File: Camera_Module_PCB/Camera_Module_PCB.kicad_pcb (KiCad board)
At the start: 2 copper layers, 84 parts, among them J1 SS-52400-002, J2 Conn_01x02, J3 FFC2A32-24-T, SW1 SW_DIP_x01, SW2 SW_Push, SW3 SW_Push, U2 ESP32-S3R8, U4 MAX98357AETE_T, Y1 40MHz

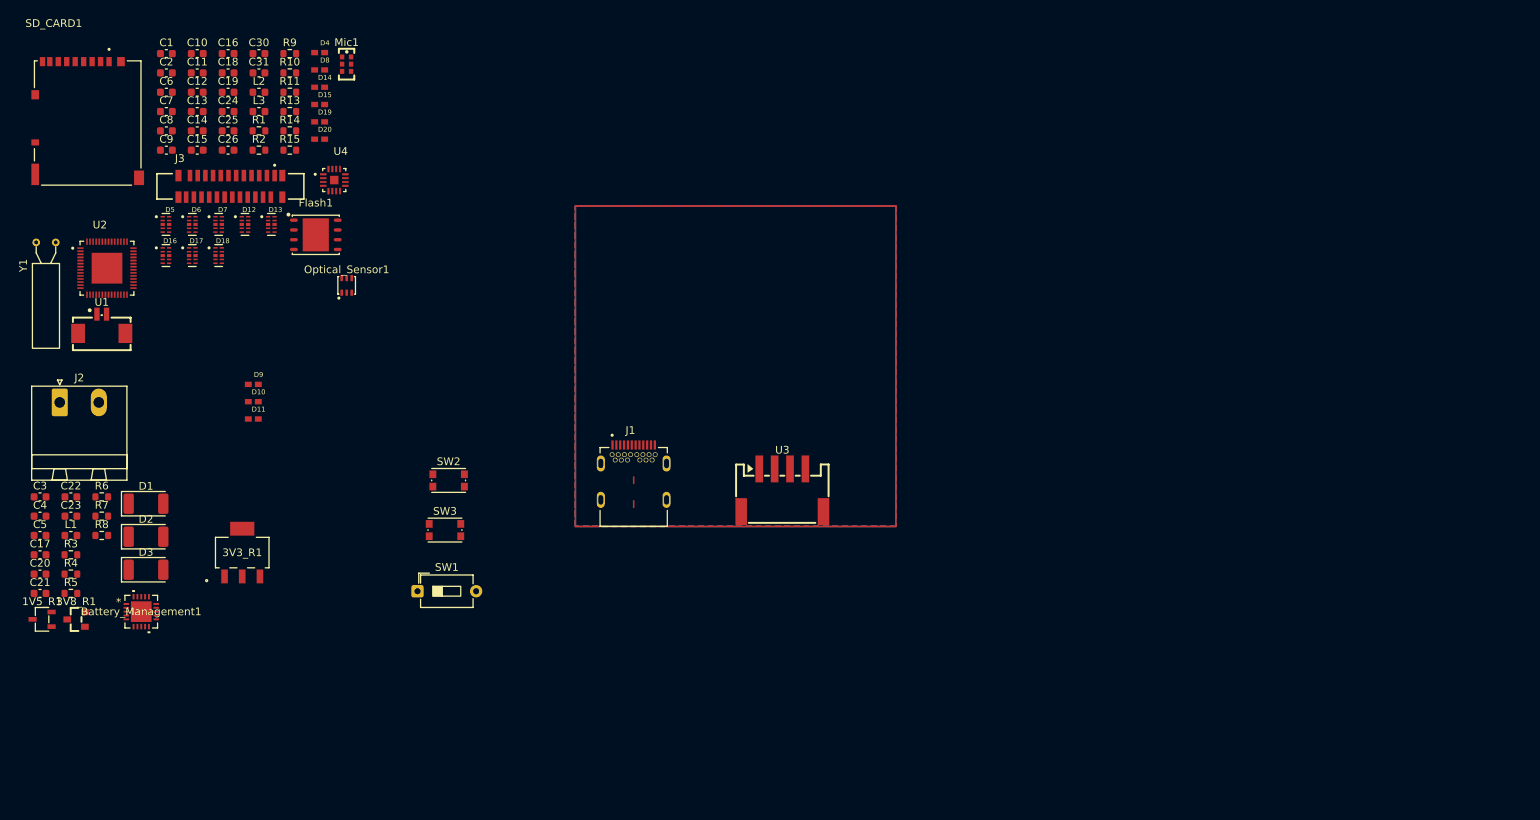
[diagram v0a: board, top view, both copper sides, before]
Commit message: Began early Layout for PCB
Moved most of the ICs into a general area layout for the PCB.
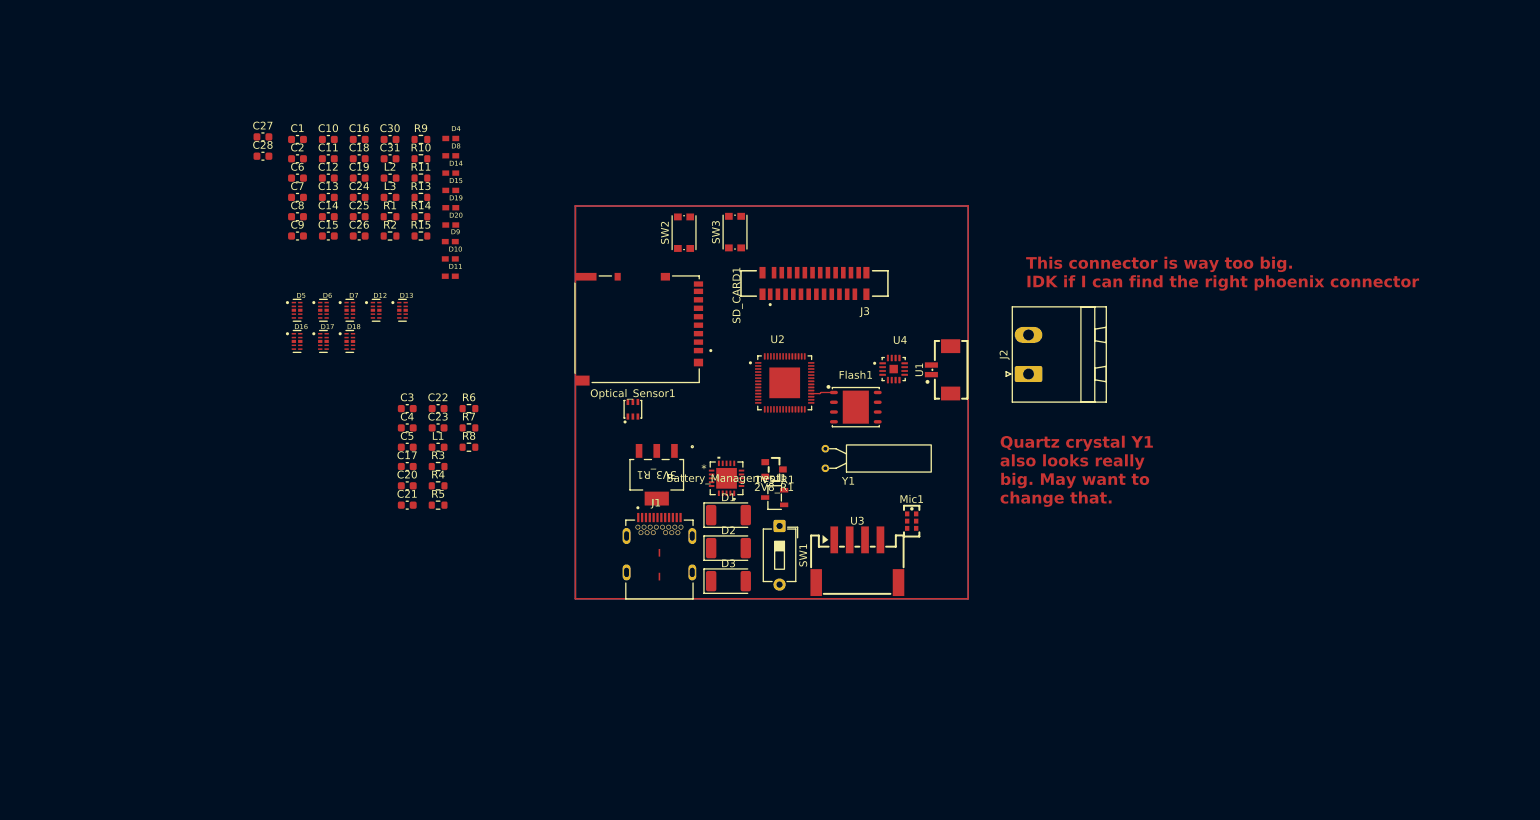
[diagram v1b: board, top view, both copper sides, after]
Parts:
- added C27: 1uF, Capacitor_SMD:C_0603_1608Metric, F.Cu at (61.0, 41.8)
- added C28: 0.1uF, Capacitor_SMD:C_0603_1608Metric, F.Cu at (61.0, 44.3)
- moved J2 126.0 mm to (160.5, 72.6), turned to 90 degrees
- moved U1 109.2 mm to (149.1, 72.1), turned to 90 degrees
- moved Y1 106.7 mm to (134.1, 84.9), turned to 90 degrees
- moved 1V5_R1 96.5 mm to (127.5, 88.7)
- moved Mic1 94.5 mm to (145.3, 91.8)
- moved 2V8_R1 92.8 mm to (127.4, 85.0), turned to 180 degrees
- moved U2 89.3 mm to (128.8, 73.8)
- moved Battery_Management1 78.0 mm to (121.2, 86.2)
- moved J3 77.0 mm to (132.7, 60.9), turned to 180 degrees
- moved U4 76.7 mm to (143.0, 72.0)
- moved SD_CARD1 76.3 mm to (109.6, 66.8), turned to -90 degrees
- moved D1 75.7 mm to (121.5, 91.0)
- moved D2 75.7 mm to (121.5, 95.3)
- moved D3 75.7 mm to (121.5, 99.6)
- moved Flash1 73.7 mm to (138.1, 77.0)
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- renumbered 3V8_R1 to 2V8_R1
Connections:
- U2 pad 29: +3.3V -> /VDD_SPI
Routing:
- net Net-(Flash1-CS): track 0.00 -> 3.01 mm
- removed copper zone on B.Cu, net GND
- removed copper zone on F.Cu, net GND
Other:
- copper layers 2 -> 4
- board text added: "Quartz crystal Y1 also looks really big. May want to change that."
- board text added: "This connector is way too big. IDK if I can find the right phoenix connector"

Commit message: Finished Schematic Except for a small few passives
Finished all of the connections in the schematic page and added a new LED driver. A small selection of passive elements must be given proper values after some calculations.
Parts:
- added C29: 4.7u, Capacitor_SMD:C_0603_1608Metric, F.Cu at (121.0, 40.7)
- added C32: 10uF, Capacitor_SMD:C_0603_1608Metric, F.Cu at (110.0, 40.7)
- added C33: 1uF, Capacitor_SMD:C_0603_1608Metric, F.Cu at (110.0, 43.2)
- added D21: D_Zener, Diode_SMD:D_0603_1608Metric, F.Cu at (47.2, 60.1)
- added D22: LED, LED_SMD:LED_2010_5025Metric, F.Cu at (48.9, 52.4)
- added D23: LED, LED_SMD:LED_2010_5025Metric, F.Cu at (48.9, 56.7)
- added L4: 6.8u, Inductor_SMD:L_0603_1608Metric, F.Cu at (110.0, 45.7)
- added R12: 1k, Resistor_SMD:R_0603_1608Metric, F.Cu at (121.0, 43.2)
- added R16: 25k, Resistor_SMD:R_0603_1608Metric, F.Cu at (121.0, 45.7)
- added R17: Riset, Resistor_SMD:R_0603_1608Metric, F.Cu at (51.2, 60.1)
- added TH1: 10k, Resistor_SMD:R_0603_1608Metric, F.Cu at (57.2, 51.5)
- added U5: AP3032KTR-G1, AP3032KTR-G1:SOT23-6_DIO, F.Cu at (131.5, 42.8)
- D1, D2, D3: footprint LED_SMD:LED_2010_5025Metric -> LED_SMD:LED_0603_1608Metric
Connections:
- Battery_Management1 pad 1: /Power Supply/Charge_Out -> V_OUT_BM
- Battery_Management1 pad 10: unconnected-(Battery_Management1-VSS-Pad10) -> GND
- Battery_Management1 pad 11: unconnected-(Battery_Management1-VSS-Pad11) -> GND
- Battery_Management1 pad 12: unconnected-(Battery_Management1-PROG3-Pad12) -> Net-(Battery_Management1-PROG3)
- Battery_Management1 pad 13: unconnected-(Battery_Management1-PROG1-Pad13) -> Net-(Battery_Management1-PROG1)
- Battery_Management1 pad 21: unconnected-(Battery_Management1-EP-Pad21) -> GND
- Battery_Management1 pad 5: unconnected-(Battery_Management1-THERM-Pad5) -> Net-(Battery_Management1-THERM)
- U2 pad 38: unconnected-(U2-GPIO33-Pad38) -> /LED_CT

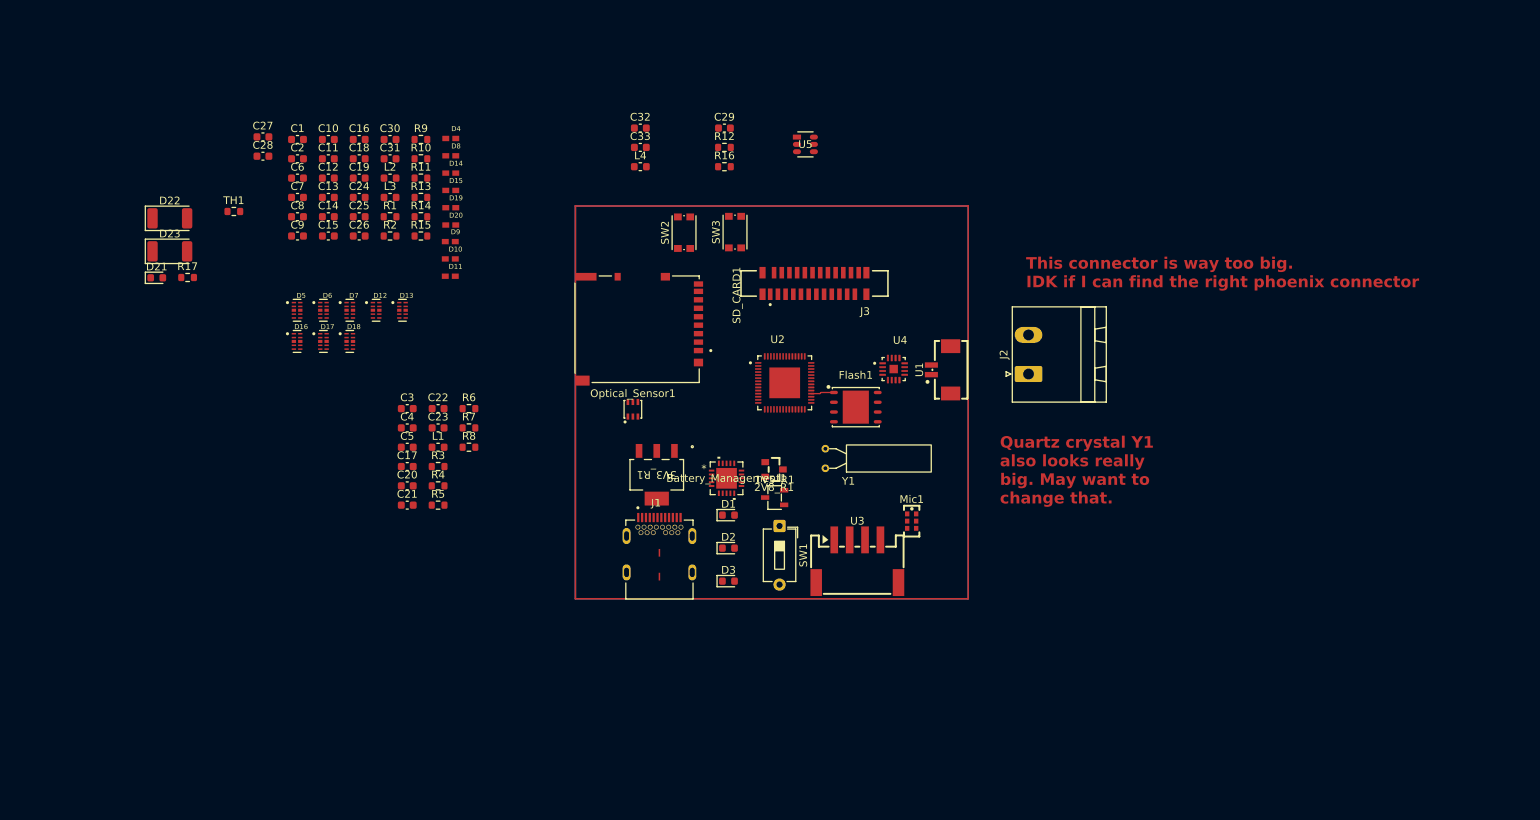
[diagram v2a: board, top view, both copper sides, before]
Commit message: Added Most ICs to the General PCB Layout
Most of the intended ICs that are going to be used were put into a general IC layout. A decision will need to be made in regards to the antenna. The ESP32 Model that is being used may be replaced, or remain the same.
Once the decision is made, more can be added.
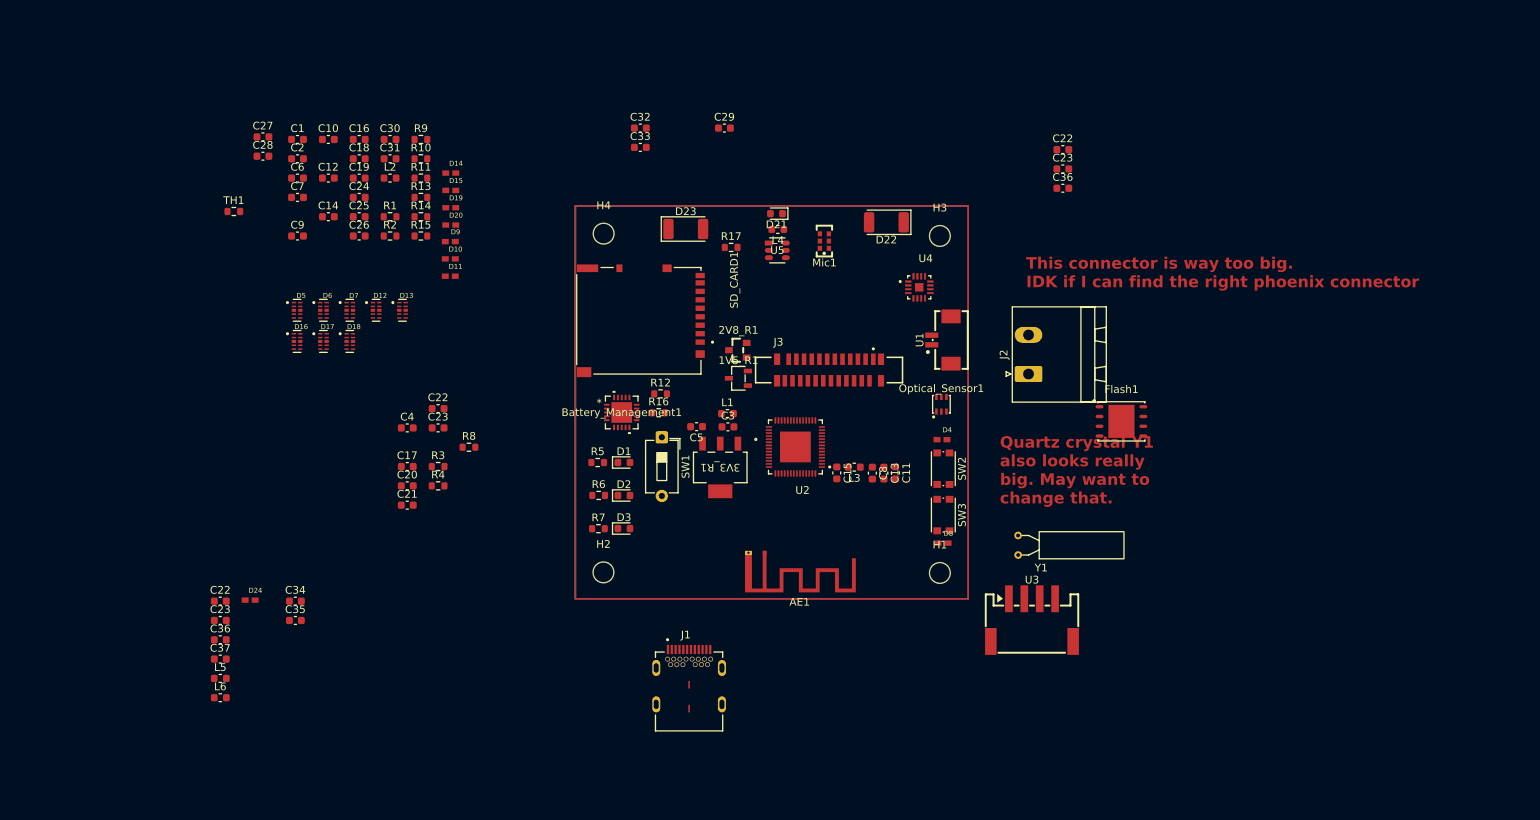
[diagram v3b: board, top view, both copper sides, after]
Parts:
- added AE1: Antenna, RF_Antenna:Texas_SWRA117D_2.4GHz_Left, F.Cu at (126.2, 95.9)
- added C22: C_Small, Capacitor_SMD:C_0603_1608Metric, F.Cu at (55.5, 102.2)
- added C22: NG, Capacitor_SMD:C_0603_1608Metric, F.Cu at (165.0, 43.5)
- added C23: C_Small, Capacitor_SMD:C_0603_1608Metric, F.Cu at (55.5, 104.7)
- added C23: 1.8pF, Capacitor_SMD:C_0603_1608Metric, F.Cu at (165.0, 46.0)
- added C34: 1 uF, Capacitor_SMD:C_0603_1608Metric, F.Cu at (65.2, 102.2)
- added C35: 100 nF, Capacitor_SMD:C_0603_1608Metric, F.Cu at (65.2, 104.7)
- added C36: 1pF, Capacitor_SMD:C_0603_1608Metric, F.Cu at (165.0, 48.5)
- added C36: C_Small, Capacitor_SMD:C_0603_1608Metric, F.Cu at (55.5, 107.2)
- added C37: C_Small, Capacitor_SMD:C_0603_1608Metric, F.Cu at (55.5, 109.7)
- added D24: 0402ESDA-MLP1, ESP32CAM_Foorprints:ESD_0402ESDA-MLP1, F.Cu at (59.3, 102.0)
- added H1: MountingHole, MountingHole:MountingHole_2.7mm, F.Cu at (149.0, 98.5)
- added H2: MountingHole, MountingHole:MountingHole_2.7mm, F.Cu at (105.2, 98.4)
- added H3: MountingHole, MountingHole:MountingHole_2.7mm, F.Cu at (149.0, 54.7)
- added H4: MountingHole, MountingHole:MountingHole_2.7mm, F.Cu at (105.3, 54.4)
- added L5: L, Inductor_SMD:L_0603_1608Metric, F.Cu at (55.5, 112.2)
- added L6: L, Inductor_SMD:L_0603_1608Metric, F.Cu at (55.5, 114.7)
- R17: value Riset -> 10
- moved D22 93.1 mm to (142.0, 52.9), turned to 180 degrees
- moved C11 84.3 mm to (143.2, 85.5), turned to -90 degrees
- moved C8 81.8 mm to (140.2, 85.5), turned to -90 degrees
- moved D8 81.4 mm to (149.4, 94.6)
- moved D21 81.0 mm to (127.7, 51.8), turned to 180 degrees
- moved C13 80.6 mm to (141.7, 85.5), turned to -90 degrees
- moved D4 74.9 mm to (149.2, 81.2)
- moved C15 72.9 mm to (135.6, 85.5), turned to -90 degrees
- moved R17 70.8 mm to (121.8, 56.2)
- moved L3 69.8 mm to (137.8, 84.8), turned to 180 degrees
- moved D23 67.1 mm to (116.0, 53.8)
- moved SW3 45.7 mm to (149.4, 91.0), turned to -90 degrees
- moved SW2 45.6 mm to (149.4, 85.0), turned to -90 degrees
- moved C3 41.7 mm to (121.4, 79.5)
- moved Optical_Sensor1 40.1 mm to (149.2, 76.6)
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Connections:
- 1V5_R1 pad 2: /Power Supply/VDD_1V5 -> VDD_1V5
- 2V8_R1 pad 2: +3.3V -> AVDD_2V8
- 2V8_R1 pad 3: /Power Supply/AVDD_2V8 -> +3.3V
- D10 pad 1: /Power Supply/USB_D+ -> /USB_D+
- D19 pad 2: Net-(U2-U0RXD) -> Net-(U2-U0TXD)
- D9 pad 1: /Power Supply/USB_D- -> /USB_D-
- J1 pad A6: /Power Supply/USB_D+ -> /USB_D+
- J1 pad A7: /Power Supply/USB_D- -> /USB_D-
- J1 pad B6: /Power Supply/USB_D+ -> /USB_D+
- J1 pad B7: /Power Supply/USB_D- -> /USB_D-
- J3 pad 10: /VDD_1V5 -> VDD_1V5
- J3 pad 11: /AVDD_2V8 -> AVDD_2V8
- J3 pad 4: /AVDD_2V8 -> AVDD_2V8
- R13 pad 1: /AVDD_2V8 -> AVDD_2V8
- U2 pad 1: unconnected-(U2-LNA_IN-Pad1) -> /LNA_IN
- U2 pad 37: /IR_DIM -> /LED_CT
- U2 pad 38: /LED_CT -> unconnected-(U2-GPIO33-Pad38)
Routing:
- net Net-(Flash1-CS): track 3.01 -> 0.00 mm
- added copper zone on In1.Cu, net GND
- added copper zone on In2.Cu, net GND

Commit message: MCU Layout Started
The layout for the ESP32 has been started, according to the recommended 4-Layer layout. Please look over the antenna and continue layout.
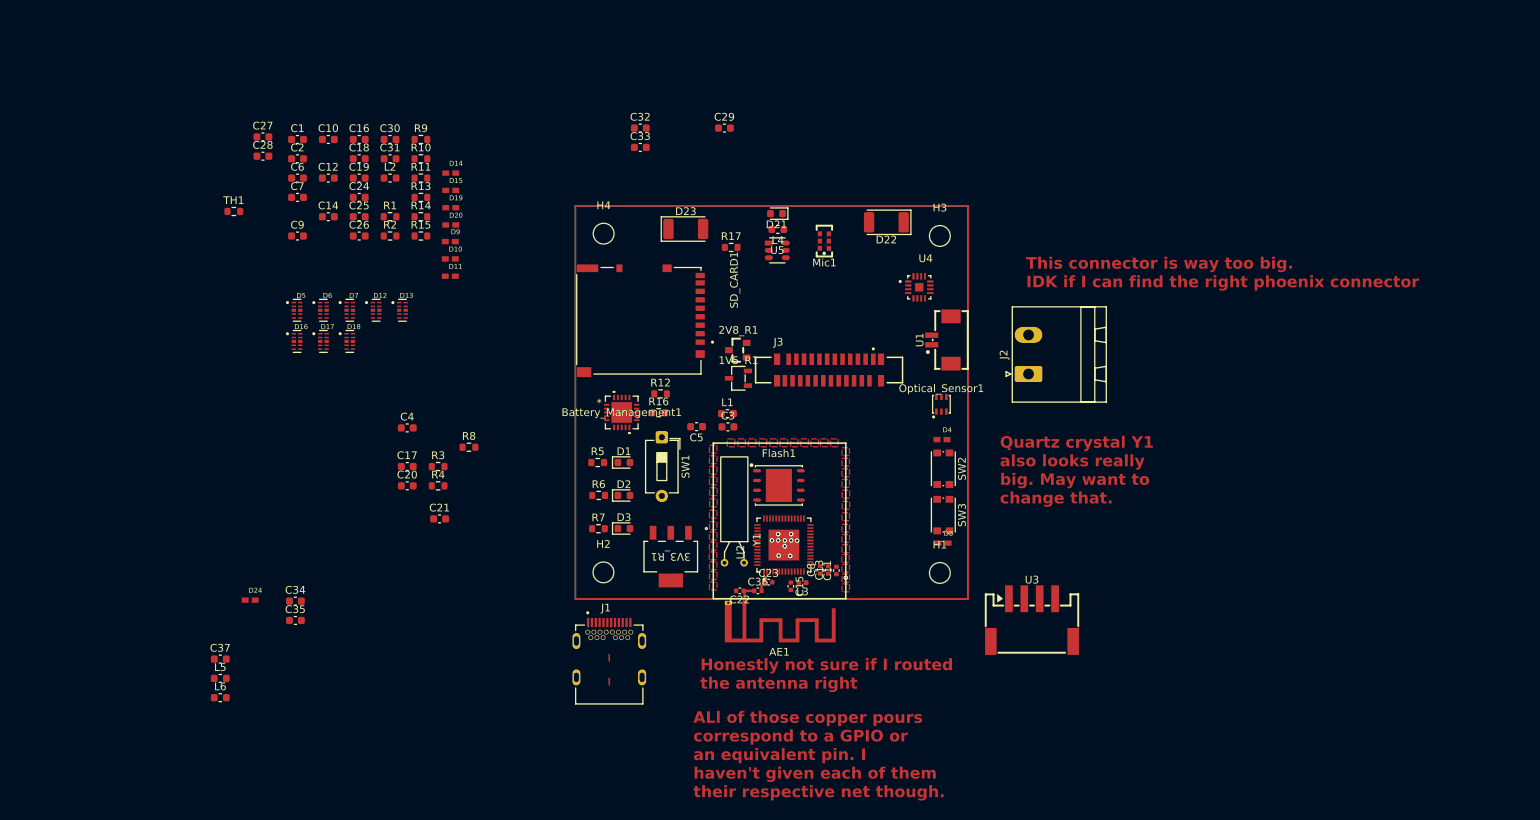
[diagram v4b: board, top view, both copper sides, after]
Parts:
- removed the C22 at (83.8, 77.1)
- removed the C22 at (55.5, 102.2)
- removed the C23 at (55.5, 104.7)
- removed the C23 at (83.8, 79.7)
- removed the C36 at (55.5, 107.2)
- C11, C13, C15, C22, C23, C36, C8: footprint Capacitor_SMD:C_0603_1608Metric -> Capacitor_SMD:C_0402_1005Metric
- L3: footprint Inductor_SMD:L_0603_1608Metric -> Inductor_SMD:L_0402_1005Metric
- moved C22 71.1 mm to (123.0, 100.8), turned to 180 degrees
- moved C23 65.9 mm to (126.7, 99.7)
- moved C36 65.6 mm to (125.3, 100.8)
- moved Flash1 45.3 mm to (128.1, 87.1)
- moved Y1 35.6 mm to (123.5, 97.2), turned to 180 degrees
- moved L3 16.5 mm to (131.1, 99.8)
- moved C15 15.9 mm to (129.6, 100.2)
- moved C11 14.8 mm to (135.5, 98.2), turned to 90 degrees
- moved C13 14.5 mm to (134.5, 98.1), turned to 90 degrees
- moved C8 14.3 mm to (133.4, 98.1), turned to 90 degrees
- moved 3V3_R1 13.3 mm to (114.0, 96.4)
- moved U2 12.8 mm to (128.7, 94.9), turned to 90 degrees
- moved J1 11.0 mm to (106.0, 112.1)
- moved AE1 7.01 mm to (123.6, 102.4)
- moved C21 4.56 mm to (84.0, 91.5)
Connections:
- AE1 pad 2: (no net) -> GND
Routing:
- net Net-(AE1-A): track 0.00 -> 3.00 mm
- net /LNA_IN: track 0.00 -> 2.75 mm
- net GND: vias 0 -> 10
- net +3.3V: vias 0 -> 1
- added copper zone on F.Cu, net +3.3V
- added copper zone on In2.Cu, net +3.3V
- added copper zone on F.Cu, net /RST
- added copper zone on F.Cu, net GND
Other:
- board text added: "ALl of those copper pours correspond to a GPIO or an equivalent pin. I haven't given each of them their respective net though."
- board text added: "Honestly not sure if I routed the antenna right"
